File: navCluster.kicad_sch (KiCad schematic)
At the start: 0 parts

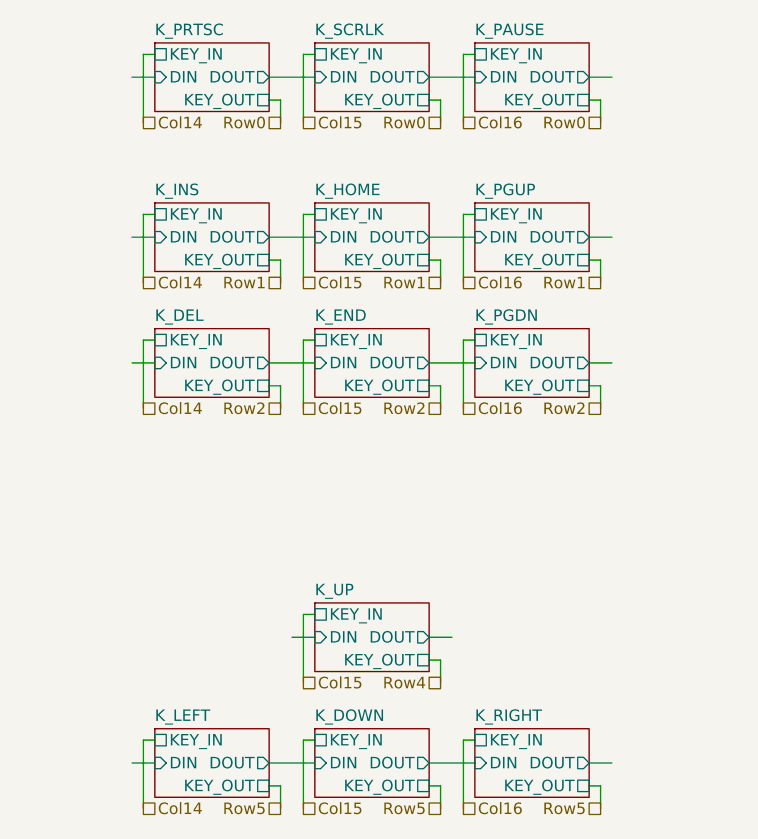
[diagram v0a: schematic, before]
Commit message: Unified key sch pages
One large page is simpler in this case
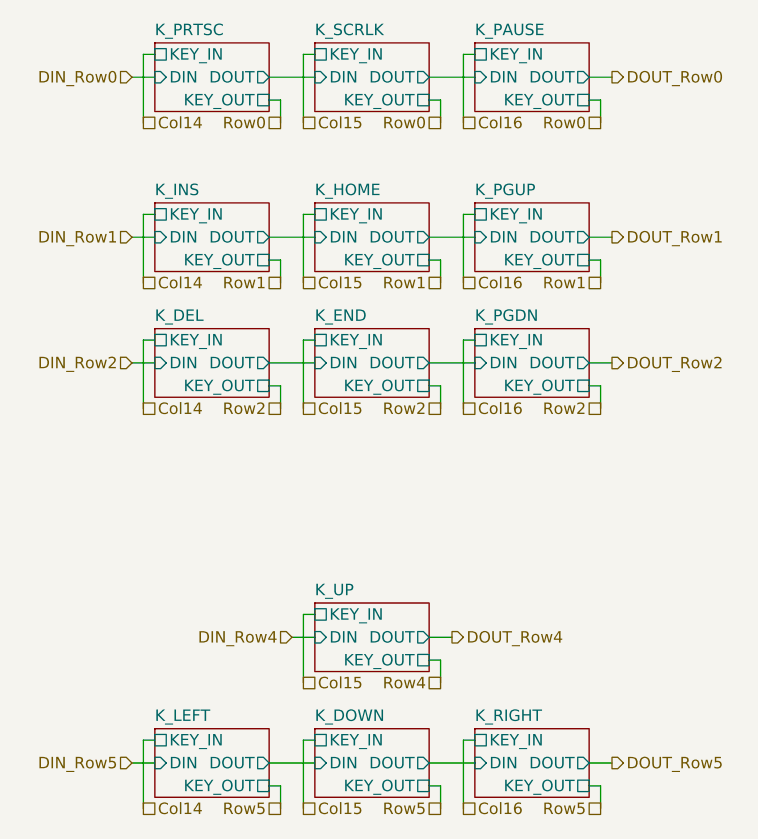
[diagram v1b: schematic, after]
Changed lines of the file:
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@@
+		)
+	)
+	(hierarchical_label "DOUT_Row0"
+		(shape output)
+		(at 171.45 55.88 0)
+		(effects
+			(font
+				(size 1.27 1.27)
+			)
+			(justify left)
 		)
 	)
@@
 		)
 	)
+	(hierarchical_label "DOUT_Row4"
+		(shape output)
+		(at 153.67 118.11 0)
+		(effects
+			(font
+				(size 1.27 1.27)
+			)
+			(justify left)
+		)
+	)
 	(hierarchical_label "Col15"
 		(shape passive)
@@
 		)
 	)
+	(hierarchical_label "DIN_Row1"
+		(shape input)
+		(at 118.11 73.66 180)
+		(effects
+			(font
+				(size 1.27 1.27)
+			)
+			(justify right)
+		)
+	)
 	(hierarchical_label "Row0"
 		(shape passive)
@@
 		)
 	)
+	(hierarchical_label "DIN_Row0"
+		(shape input)
+		(at 118.11 55.88 180)
+		(effects
+			(font
+				(size 1.27 1.27)
+			)
+			(justify right)
+		)
+	)
 	(hierarchical_label "Row2"
 		(shape passive)
@@
 		)
 	)
+	(hierarchical_label "DOUT_Row1"
+		(shape output)
+		(at 171.45 73.66 0)
+		(effects
+			(font
+				(size 1.27 1.27)
+			)
+			(justify left)
+		)
+	)
 	(hierarchical_label "Row1"
 		(shape passive)
@@
 		)
 	)
+	(hierarchical_label "DIN_Row4"
+		(shape input)
+		(at 135.89 118.11 180)
+		(effects
+			(font
+				(size 1.27 1.27)
+			)
+			(justify right)
+		)
+	)
+	(hierarchical_label "DOUT_Row2"
+		(shape output)
+		(at 171.45 87.6392 0)
+		(effects
+			(font
+				(size 1.27 1.27)
+			)
+			(justify left)
+		)
+	)
+	(hierarchical_label "DIN_Row5"
+		(shape input)
+		(at 118.11 132.08 180)
+		(effects
+			(font
+				(size 1.27 1.27)
+			)
+			(justify right)
+		)
+	)
 	(hierarchical_label "Row1"
 		(shape passive)
@@
 		)
 	)
+	(hierarchical_label "DOUT_Row5"
+		(shape output)
+		(at 171.45 132.08 0)
+		(effects
+			(font
+				(size 1.27 1.27)
+			)
+			(justify left)
+		)
+	)
 	(hierarchical_label "Row2"
 		(shape passive)
@@
 		(effects
 			(font
+				(size 1.27 1.27)
+			)
+			(justify right)
+		)
+	)
+	(hierarchical_label "DIN_Row2"
+		(shape input)
+		(at 118.11 87.63 180)
+		(effects
+			(font
